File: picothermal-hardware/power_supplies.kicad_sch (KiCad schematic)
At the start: 42 parts, among them U2 AP7330-W5-7, U3 AP7330-W5-7, U5 TLV62569A, U6 TLV62569A

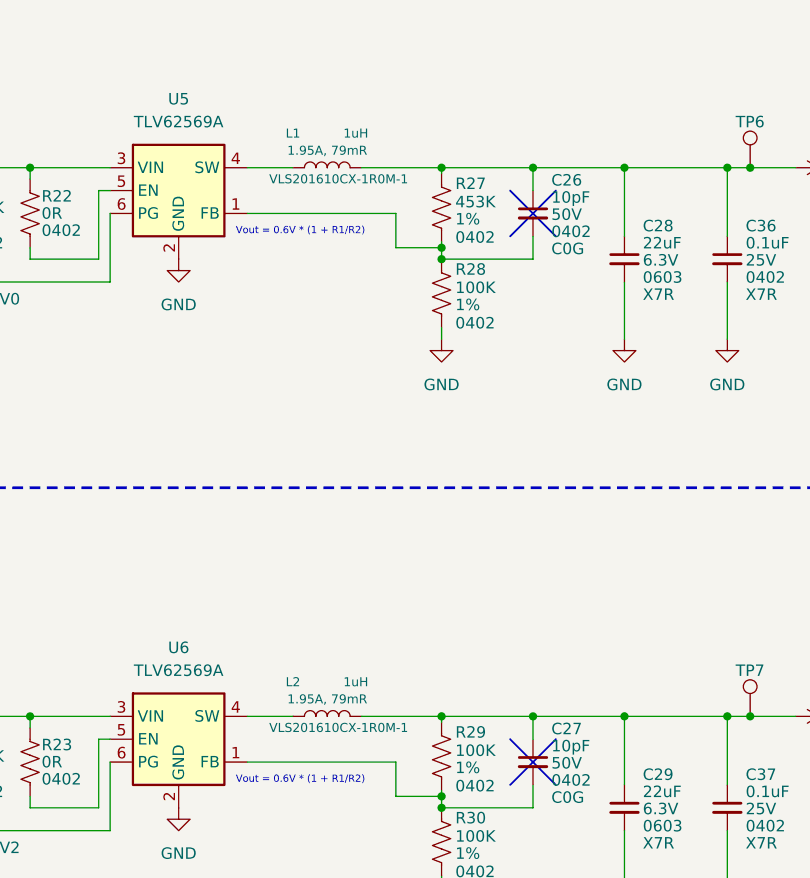
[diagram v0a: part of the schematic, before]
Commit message: Updated hardware project to work with Kicad 7.0
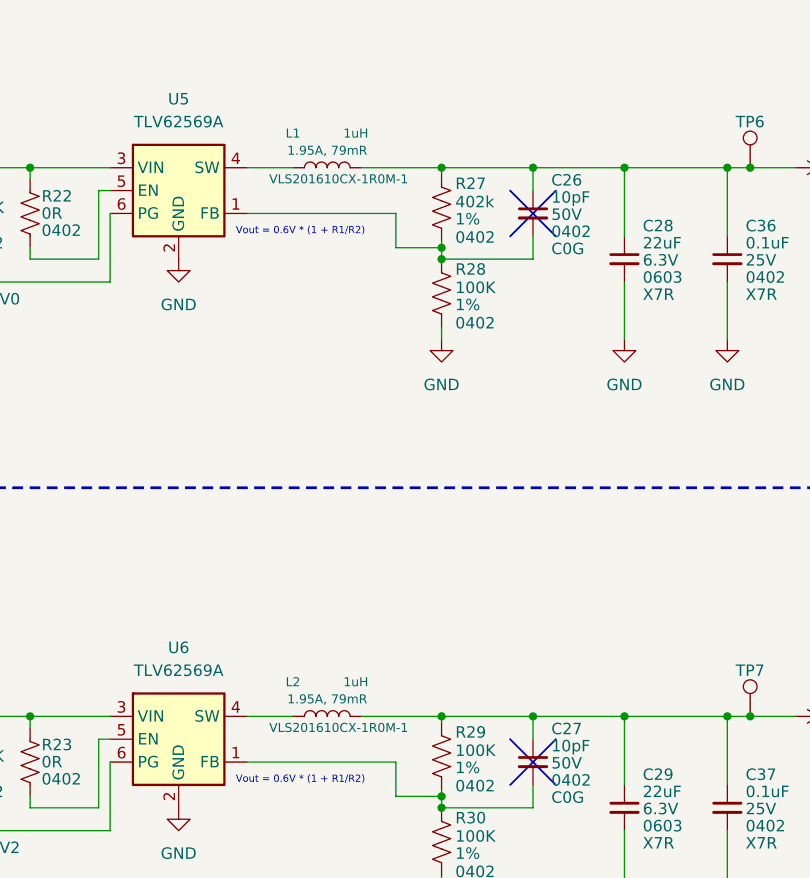
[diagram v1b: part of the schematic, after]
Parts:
- R27: value 453K -> 402k
